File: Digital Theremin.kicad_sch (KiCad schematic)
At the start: 37 parts, among them J1 Conn_01x02_Female, J2 AudioJack3, J3 USB_B_Micro, J4 Conn_01x03_Female, SW1 SW_Push, SW2 SW_Push, SW3 SW_SPDT, U1 AP2204K-3.0, U2 TDA2822

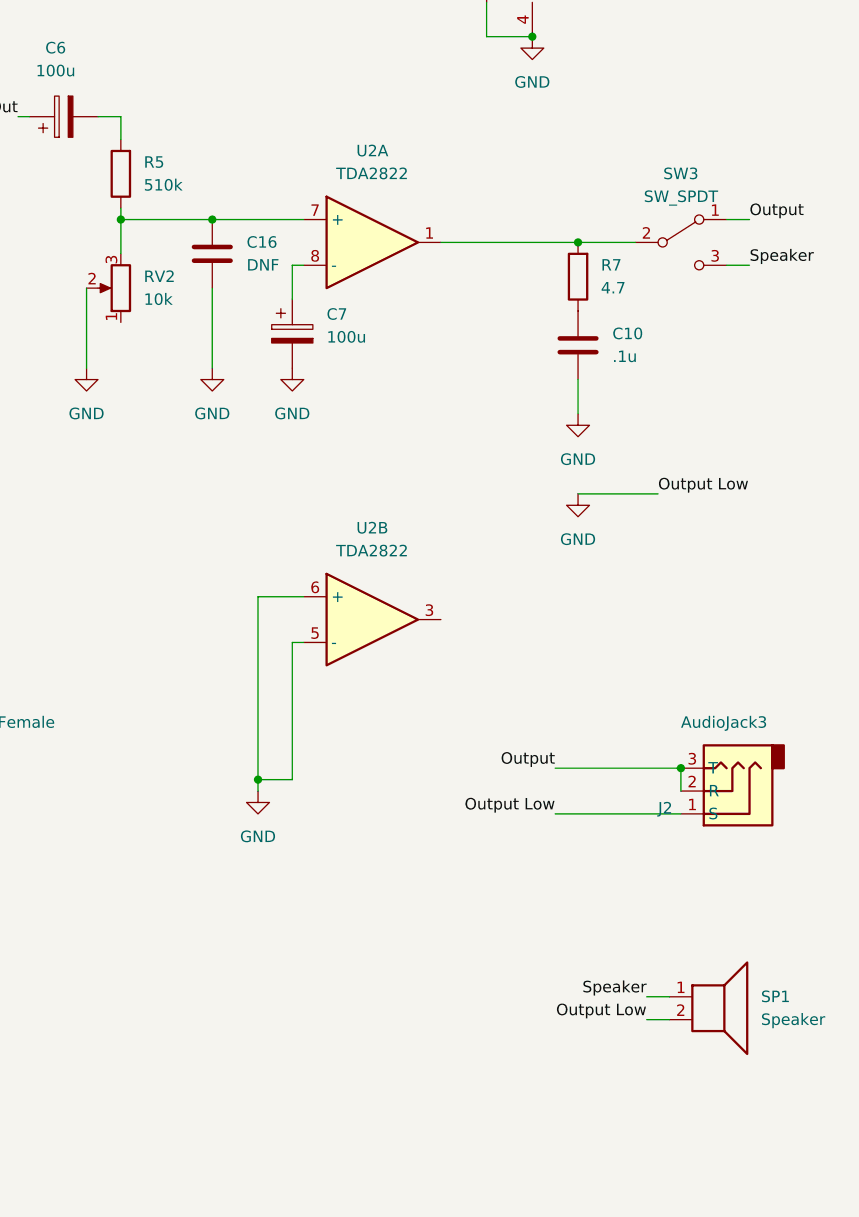
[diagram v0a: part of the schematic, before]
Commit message: Single ended layout
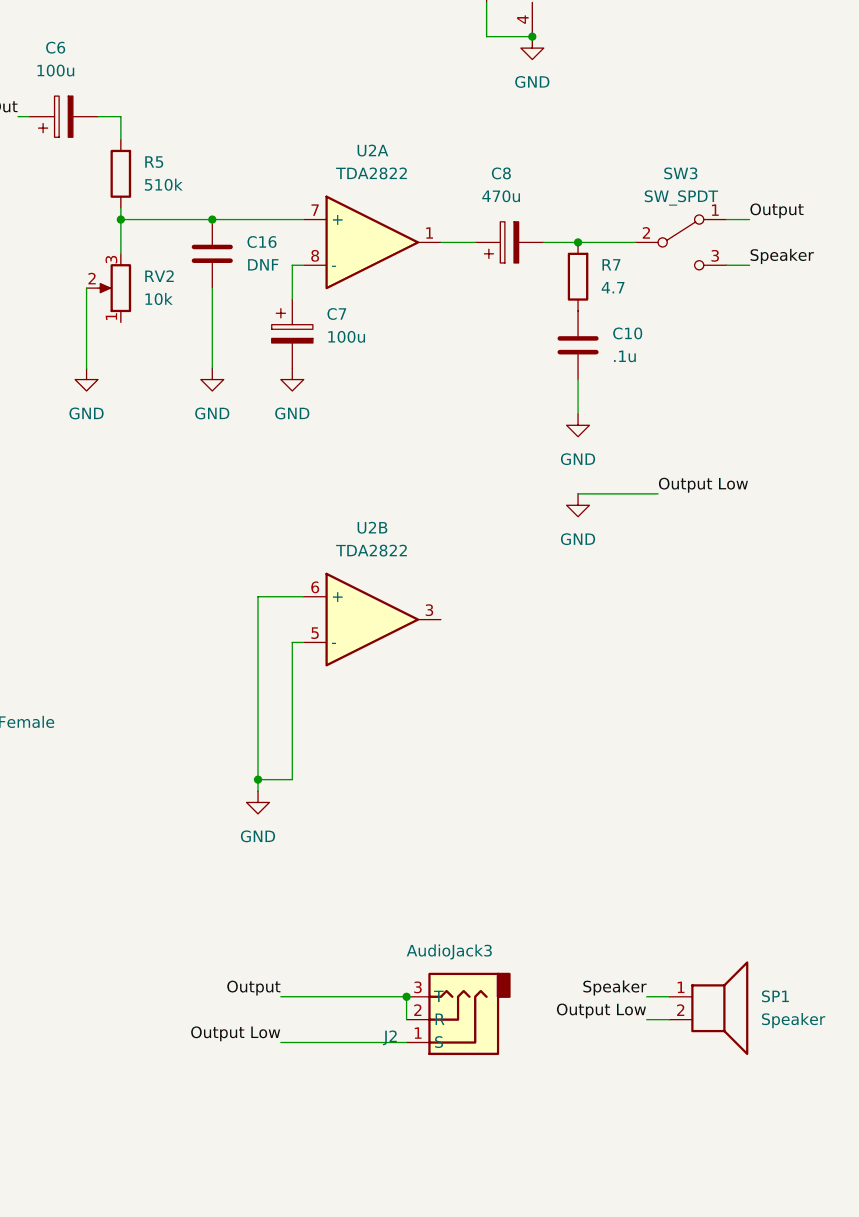
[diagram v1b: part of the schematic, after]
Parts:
- added C8: 470u, Capacitor_THT:CP_Radial_D5.0mm_P2.50mm, symbol Device:C_Polarized
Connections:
- net at R7.2, SW3.2 (B): now also C8.2; no longer U2.1
- new net: C8.1, U2.1
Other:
- moved on the sheet: J2
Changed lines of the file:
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@@
 (kicad_sch (version 20211123) (generator eeschema)
   (paper "A4")
+  (junction (at 127 38.1) (diameter 0) (color 0 0 0 0)
+  )
+  (junction (at 44.45 180.34) (diameter 0) (color 0 0 0 0)
+  )
+  (junction (at 228.6 144.78) (diameter 0) (color 0 0 0 0)
+  )
+  (junction (at 237.49 22.86) (diameter 0) (color 0 0 0 0)
+  )
+  (junction (at 121.92 156.21) (diameter 0) (color 0 0 0 0)
+  )
+  (junction (at 44.45 187.96) (diameter 0) (color 0 0 0 0)
+  )
+  (junction (at 242.57 38.1) (diameter 0) (color 0 0 0 0)
+  )
+  (junction (at 196.85 58.42) (diameter 0) (color 0 0 0 0)
+  )
+  (junction (at 156.21 156.21) (diameter 0) (color 0 0 0 0)
+  )
+  (junction (at 26.67 128.27) (diameter 0) (color 0 0 0 0)
+  )
+  (junction (at 26.67 163.83) (diameter 0) (color 0 0 0 0)
+  )
+  (junction (at 166.37 156.21) (diameter 0) (color 0 0 0 0)
+  )
+  (junction (at 45.72 45.72) (diameter 0) (color 0 0 0 0)
+  )
+  (junction (at 49.53 107.95) (diameter 0) (color 0 0 0 0)
+  )
+  (junction (at 26.67 107.95) (diameter 0) (color 0 0 0 0)
+  )
+  (junction (at 26.67 146.05) (diameter 0) (color 0 0 0 0)
+  )
   (junction (at 247.65 60.96) (diameter 0) (color 0 0 0 0)
   )
-  (junction (at 127 38.1) (diameter 0) (color 0 0 0 0)
-  )
-  (junction (at 44.45 180.34) (diameter 0) (color 0 0 0 0)
-  )
-  (junction (at 259.08 119.38) (diameter 0) (color 0 0 0 0)
-  )
-  (junction (at 237.49 22.86) (diameter 0) (color 0 0 0 0)
-  )
-  (junction (at 121.92 156.21) (diameter 0) (color 0 0 0 0)
-  )
-  (junction (at 44.45 187.96) (diameter 0) (color 0 0 0 0)
-  )
-  (junction (at 242.57 38.1) (diameter 0) (color 0 0 0 0)
-  )
-  (junction (at 196.85 58.42) (diameter 0) (color 0 0 0 0)
-  )
-  (junction (at 156.21 156.21) (diameter 0) (color 0 0 0 0)
-  )
-  (junction (at 26.67 128.27) (diameter 0) (color 0 0 0 0)
-  )
-  (junction (at 26.67 163.83) (diameter 0) (color 0 0 0 0)
-  )
-  (junction (at 166.37 156.21) (diameter 0) (color 0 0 0 0)
-  )
-  (junction (at 45.72 45.72) (diameter 0) (color 0 0 0 0)
-  )
-  (junction (at 49.53 107.95) (diameter 0) (color 0 0 0 0)
-  )
-  (junction (at 26.67 107.95) (diameter 0) (color 0 0 0 0)
-  )
-  (junction (at 26.67 146.05) (diameter 0) (color 0 0 0 0)
-  )
   (junction (at 212.09 120.65) (diameter 0) (color 0 0 0 0)
   )
@@
     (stroke (width 0) (type default) (color 0 0 0 0))
   )
-  (wire (pts (xy 259.08 119.38) (xy 259.08 121.92))
+  (wire (pts (xy 228.6 144.78) (xy 228.6 147.32))
     (stroke (width 0) (type default) (color 0 0 0 0))
   )
@@
     (stroke (width 0) (type default) (color 0 0 0 0))
   )
+  (wire (pts (xy 243.84 60.96) (xy 247.65 60.96))
+    (stroke (width 0) (type default) (color 0 0 0 0))
+  )
   (wire (pts (xy 128.27 156.21) (xy 134.62 156.21))
     (stroke (width 0) (type default) (color 0 0 0 0))
@@
     (stroke (width 0) (type default) (color 0 0 0 0))
   )
-  (wire (pts (xy 245.11 119.38) (xy 259.08 119.38))
+  (wire (pts (xy 214.63 144.78) (xy 228.6 144.78))
     (stroke (width 0) (type default) (color 0 0 0 0))
   )
@@
     (stroke (width 0) (type default) (color 0 0 0 0))
   )
-  (wire (pts (xy 232.41 60.96) (xy 247.65 60.96))
-    (stroke (width 0) (type default) (color 0 0 0 0))
-  )
   (wire (pts (xy 237.49 34.29) (xy 237.49 38.1))
     (stroke (width 0) (type default) (color 0 0 0 0))
@@
     (stroke (width 0) (type default) (color 0 0 0 0))
   )
-  (wire (pts (xy 245.11 124.46) (xy 259.08 124.46))
+  (wire (pts (xy 214.63 149.86) (xy 228.6 149.86))
     (stroke (width 0) (type default) (color 0 0 0 0))
   )
@@
   )
   (wire (pts (xy 78.74 189.23) (xy 81.28 189.23))
+    (stroke (width 0) (type default) (color 0 0 0 0))
+  )
+  (wire (pts (xy 232.41 60.96) (xy 236.22 60.96))
     (stroke (width 0) (type default) (color 0 0 0 0))
   )
@@
     (effects (font (size 1.27 1.27)) (justify left bottom))
   )
-  (label "Output" (at 245.11 119.38 180)
+  (label "Output" (at 214.63 144.78 180)
     (effects (font (size 1.27 1.27)) (justify right bottom))
   )
@@
     (effects (font (size 1.27 1.27)) (justify right bottom))
   )
-  (label "Output Low" (at 245.11 124.46 180)
+  (label "Output Low" (at 214.63 149.86 180)
     (effects (font (size 1.27 1.27)) (justify right bottom))
   )
@@
     (pin "1")
   )
+  (symbol (lib_id "Device:C_Polarized") (at 240.03 60.96 90) (unit 1)
+    (in_bom yes) (on_board yes) (fields_autoplaced)
+    (property "Reference" "C8" (id 0) (at 239.141 53.34 90))
+    (property "Value" "470u" (id 1) (at 239.141 55.88 90))
+    (property "Footprint" "Capacitor_THT:CP_Radial_D5.0mm_P2.50mm" (id 2) (at 243.84 59.9948 0)
+      (effects (font (size 1.27 1.27)) hide)
+    )
+    (property "Datasheet" "~" (id 3) (at 240.03 60.96 0)
+      (effects (font (size 1.27 1.27)) hide)
+    )
+    (pin "1")
+    (pin "2")
+  )
   (symbol (lib_id "Device:C") (at 49.53 91.44 180) (unit 1)
     (in_bom yes) (on_board yes) (fields_autoplaced)
@@
   (symbol (lib_id "power:GND") (at 247.65 88.9 0) (unit 1)
     (in_bom yes) (on_board yes) (fields_autoplaced)
-    (property "Reference" "#PWR?" (id 0) (at 247.65 95.25 0)
+    (property "Reference" "#PWR0109" (id 0) (at 247.65 95.25 0)
       (effects (font (size 1.27 1.27)) hide)
     )
@@
   (symbol (lib_id "power:GND") (at 215.9 74.93 0) (unit 1)
     (in_bom yes) (on_board yes)
-    (property "Reference" "#PWR?" (id 0) (at 215.9 81.28 0)
+    (property "Reference" "#PWR0108" (id 0) (at 215.9 81.28 0)
       (effects (font (size 1.27 1.27)) hide)
     )
@@
     (pin "1")
   )
-  (symbol (lib_id "Connector:AudioJack3") (at 264.16 121.92 180) (unit 1)
+  (symbol (lib_id "Connector:AudioJack3") (at 233.68 147.32 180) (unit 1)
     (in_bom yes) (on_board yes)
-    (property "Reference" "J2" (id 0) (at 256.54 123.8251 0)
-      (effects (font (size 1.27 1.27)) (justify right))
-    )
-    (property "Value" "AudioJack3" (id 1) (at 259.08 114.3 0)
-      (effects (font (size 1.27 1.27)) (justify right))
-    )
-    (property "Footprint" "Connector_PinHeader_2.54mm:PinHeader_1x03_P2.54mm_Vertical" (id 2) (at 264.16 121.92 0)
-      (effects (font (size 1.27 1.27)) hide)
-    )
-    (property "Datasheet" "~" (id 3) (at 264.16 121.92 0)
+    (property "Reference" "J2" (id 0) (at 226.06 149.2251 0)
+      (effects (font (size 1.27 1.27)) (justify right))
+    )
+    (property "Value" "AudioJack3" (id 1) (at 228.6 139.7 0)
+      (effects (font (size 1.27 1.27)) (justify right))
+    )
+    (property "Footprint" "Connector_PinHeader_2.54mm:PinHeader_1x03_P2.54mm_Vertical" (id 2) (at 233.68 147.32 0)
+      (effects (font (size 1.27 1.27)) hide)
+    )
+    (property "Datasheet" "~" (id 3) (at 233.68 147.32 0)
       (effects (font (size 1.27 1.27)) hide)
     )
@@
       (reference "#PWR0107") (unit 1) (value "GND") (footprint "")
     )
+    (path "/ed579c80-a49d-43c2-b063-1243faa1bdc0"
+      (reference "#PWR0108") (unit 1) (value "GND") (footprint "")
+    )
     (path "/b1666e4c-8959-4256-9481-009c70d30fca"
-      (reference "#PWR?") (unit 1) (value "GND") (footprint "")
-    )
-    (path "/ed579c80-a49d-43c2-b063-1243faa1bdc0"
-      (reference "#PWR?") (unit 1) (value "GND") (footprint "")
+      (reference "#PWR0109") (unit 1) (value "GND") (footprint "")
     )
     (path "/1cc4a702-19b7-49a9-8fdf-c6c293ed93ba"
@@
       (reference "C7") (unit 1) (value "100u") (footprint "Capacitor_THT:CP_Radial_D5.0mm_P2.50mm")
     )
+    (path "/3b09ab4d-822a-42b7-ac2b-dc92ae5c85a4"
+      (reference "C8") (unit 1) (value "470u") (footprint "Capacitor_THT:CP_Radial_D5.0mm_P2.50mm")
+    )
     (path "/212a8d24-615a-4e7e-9e31-a73159e08897"

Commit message: Antenna mounts
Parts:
- removed J2: AudioJack3, Connector_PinHeader_2.54mm:PinHeader_1x03_P2.54mm_Vertical, symbol Connector:AudioJack3
- added J2: AudioJack3_Dual_Switch, Connector_Audio:Jack_3.5mm_CUI_SJ1-3525N_Horizontal, symbol Connector:AudioJack3_Dual_Switch
- ANT1, ANT2: footprint Connector_PinHeader_2.54mm:PinHeader_1x01_P2.54mm_Vertical -> MountingHole:MountingHole_3.2mm_M3_Pad_Via; PN (none) -> PRT-09739
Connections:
- net GND: now also J2.S
- net Output: now also J2.R, J2.T
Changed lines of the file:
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@@
   (junction (at 44.45 180.34) (diameter 0) (color 0 0 0 0)
   )
-  (junction (at 228.6 144.78) (diameter 0) (color 0 0 0 0)
-  )
   (junction (at 237.49 22.86) (diameter 0) (color 0 0 0 0)
   )
@@
   (junction (at 127 48.26) (diameter 0) (color 0 0 0 0)
   )
+  (junction (at 228.6 147.32) (diameter 0) (color 0 0 0 0)
+  )
   (junction (at 128.27 156.21) (diameter 0) (color 0 0 0 0)
   )
@@
     (stroke (width 0) (type default) (color 0 0 0 0))
   )
+  (wire (pts (xy 228.6 147.32) (xy 229.87 147.32))
+    (stroke (width 0) (type default) (color 0 0 0 0))
+  )
   (wire (pts (xy 214.63 144.78) (xy 228.6 144.78))
     (stroke (width 0) (type default) (color 0 0 0 0))
@@
     (stroke (width 0) (type default) (color 0 0 0 0))
   )
-  (wire (pts (xy 214.63 149.86) (xy 228.6 149.86))
+  (wire (pts (xy 214.63 157.48) (xy 229.87 157.48))
     (stroke (width 0) (type default) (color 0 0 0 0))
   )
@@
     (stroke (width 0) (type default) (color 0 0 0 0))
   )
+  (wire (pts (xy 228.6 152.4) (xy 229.87 152.4))
+    (stroke (width 0) (type default) (color 0 0 0 0))
+  )
   (wire (pts (xy 44.45 179.07) (xy 44.45 180.34))
     (stroke (width 0) (type default) (color 0 0 0 0))
@@
   )
   (wire (pts (xy 121.92 106.68) (xy 127 106.68))
+    (stroke (width 0) (type default) (color 0 0 0 0))
+  )
+  (wire (pts (xy 228.6 147.32) (xy 228.6 152.4))
     (stroke (width 0) (type default) (color 0 0 0 0))
   )
@@
     (effects (font (size 1.27 1.27)) (justify right bottom))
   )
-  (label "Output Low" (at 214.63 149.86 180)
+  (label "Output Low" (at 214.63 157.48 180)
     (effects (font (size 1.27 1.27)) (justify right bottom))
   )
@@
       (effects (font (size 1.27 1.27)) (justify left))
     )
-    (property "Footprint" "Connector_PinHeader_2.54mm:PinHeader_1x01_P2.54mm_Vertical" (id 2) (at 91.44 33.02 0)
+    (property "Footprint" "MountingHole:MountingHole_3.2mm_M3_Pad_Via" (id 2) (at 91.44 33.02 0)
       (effects (font (size 1.27 1.27)) hide)
     )
     (property "Datasheet" "~" (id 3) (at 91.44 33.02 0)
+      (effects (font (size 1.27 1.27)) hide)
+    )
+    (property "PN" "PRT-09739" (id 4) (at 91.44 33.02 0)
       (effects (font (size 1.27 1.27)) hide)
     )
@@
       (effects (font (size 1.27 1.27)) (justify left))
     )
-    (property "Footprint" "Connector_PinHeader_2.54mm:PinHeader_1x01_P2.54mm_Vertical" (id 2) (at 82.55 33.02 0)
+    (property "Footprint" "MountingHole:MountingHole_3.2mm_M3_Pad_Via" (id 2) (at 82.55 33.02 0)
       (effects (font (size 1.27 1.27)) hide)
     )
     (property "Datasheet" "~" (id 3) (at 82.55 33.02 0)
+      (effects (font (size 1.27 1.27)) hide)
+    )
+    (property "PN" "PRT-09739" (id 4) (at 82.55 33.02 0)
       (effects (font (size 1.27 1.27)) hide)
     )
@@
     (pin "2")
   )
+  (symbol (lib_id "Connector:AudioJack3_Dual_Switch") (at 234.95 152.4 180) (unit 1)
+    (in_bom yes) (on_board yes) (fields_autoplaced)
+    (property "Reference" "J2" (id 0) (at 243.84 149.8599 0)
+      (effects (font (size 1.27 1.27)) (justify right))
+    )
+    (property "Value" "AudioJack3_Dual_Switch" (id 1) (at 242.57 142.24 0)
+      (effects (font (size 1.27 1.27)) (justify right))
+    )
+    (property "Footprint" "Connector_Audio:Jack_3.5mm_CUI_SJ1-3525N_Horizontal" (id 2) (at 237.49 138.43 0)
+      (effects (font (size 1.27 1.27)) hide)
+    )
+    (property "Datasheet" "~" (id 3) (at 236.22 152.4 0)
+      (effects (font (size 1.27 1.27)) hide)
+    )
+    (property "PN" "SJ1-3525NG-PI" (id 4) (at 234.95 152.4 0)
+      (effects (font (size 1.27 1.27)) hide)
+    )
+    (pin "S")
+    (pin "T")
+    (pin "R")
+    (pin "TN")
+    (pin "RN")
+    (pin "R2")
+    (pin "RN2")
+    (pin "S2")
+    (pin "T2")
+    (pin "TN2")
+  )
   (symbol (lib_id "Device:D") (at 127 41.91 270) (unit 1)
     (in_bom yes) (on_board yes) (fields_autoplaced)
@@
     (pin "1")
   )
-  (symbol (lib_id "Connector:AudioJack3") (at 233.68 147.32 180) (unit 1)
-    (in_bom yes) (on_board yes)
-    (property "Reference" "J2" (id 0) (at 226.06 149.2251 0)
-      (effects (font (size 1.27 1.27)) (justify right))
-    )
-    (property "Value" "AudioJack3" (id 1) (at 228.6 139.7 0)
-      (effects (font (size 1.27 1.27)) (justify right))
-    )
-    (property "Footprint" "Connector_PinHeader_2.54mm:PinHeader_1x03_P2.54mm_Vertical" (id 2) (at 233.68 147.32 0)
-      (effects (font (size 1.27 1.27)) hide)
-    )
-    (property "Datasheet" "~" (id 3) (at 233.68 147.32 0)
-      (effects (font (size 1.27 1.27)) hide)
-    )
-    (pin "1")
-    (pin "2")
-    (pin "3")
-  )
   (sheet (at 96.52 38.1) (size 27.94 26.67) (fields_autoplaced)
     (stroke (width 0.1524) (type solid) (color 0 0 0 0))
@@
     )
     (path "/1cc4a702-19b7-49a9-8fdf-c6c293ed93ba"
-      (reference "ANT1") (unit 1) (value "Antenna") (footprint "Connector_PinHeader_2.54mm:PinHeader_1x01_P2.54mm_Vertical")
+      (reference "ANT1") (unit 1) (value "Antenna") (footprint "MountingHole:MountingHole_3.2mm_M3_Pad_Via")
     )
     (path "/014c8690-2583-455a-9b92-a38bc09e85a4"
-      (reference "ANT2") (unit 1) (value "Antenna") (footprint "Connector_PinHeader_2.54mm:PinHeader_1x01_P2.54mm_Vertical")
+      (reference "ANT2") (unit 1) (value "Antenna") (footprint "MountingHole:MountingHole_3.2mm_M3_Pad_Via")
     )
     (path "/3dd09d18-a721-4d83-8526-113f5b175e38"
@@
       (reference "J1") (unit 1) (value "Conn_01x02_Female") (footprint "Connector_PinHeader_2.54mm:PinHeader_1x02_P2.54mm_Vertical")
     )
-    (path "/fd28db54-b345-4c57-8e5a-c5ef1eaaa0c4"
-      (reference "J2") (unit 1) (value "AudioJack3") (footprint "Connector_PinHeader_2.54mm:PinHeader_1x03_P2.54mm_Vertical")
+    (path "/49e818d5-42a4-4525-bc02-0a9174a0443e"
+      (reference "J2") (unit 1) (value "AudioJack3_Dual_Switch") (footprint "Connector_Audio:Jack_3.5mm_CUI_SJ1-3525N_Horizontal")
     )
     (path "/1165efe1-0b3f-4f9e-af7c-43013a14e782"

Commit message: Update
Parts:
- added H1, H2: MountingHole_Pad, MountingHole:MountingHole_3.7mm_Pad, symbol Mechanical:MountingHole_Pad
- added TP1, TP2: TestPoint, TestPoint:TestPoint_Loop_D2.50mm_Drill1.0mm, symbol Connector:TestPoint
- C15: value 10n -> .1u
- C6, C7: PN (none) -> ESK107M016AC3AA
- C8: PN (none) -> 860010273011
- D5, D6: symbol Device:D -> Device:D_Schottky
- J3: footprint Connector_USB:USB_Micro-B_GCT_USB3076-30-A -> Connector_USB:USB_Micro-B_Amphenol_10104110_Horizontal
- R1: value 200 -> 220
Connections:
- net GND: now also H1.1, H2.1
- net Oscillators/Pitch Antenna: now also TP1.1
- net Oscillators/Volume Antenna: now also TP2.1
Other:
- note added: "All 0.1u caps: C320C104K5R5TA7317"
- note added: "Generic SB140 Diodes"
- note added: "SparkFun PRT-09739 connectors"
- note added: "To Fit Case: 1591XXSTBU"
